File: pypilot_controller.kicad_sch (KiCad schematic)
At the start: 36 parts, among them J1 power+, J2 power-, J3 Motor A, J4 Motor B, Q1 Q_NMOS_GDS, Q2 Q_NMOS_GDS, Q3 Q_NMOS_GDS, Q4 Q_NMOS_GDS, Q5 Q_NMOS_GDS, U2 IR2101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

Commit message: Rename NCP5106B to IR2102
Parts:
- U2, U3: symbol pypilot_components:ncp5106b -> pypilot_components:IR2101
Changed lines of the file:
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@@
 	)
 	(symbol
-		(lib_id "pypilot_components:ncp5106b")
+		(lib_id "pypilot_components:IR2101")
 		(at 138.43 73.66 0)
 		(unit 1)
@@
 	)
 	(symbol
-		(lib_id "pypilot_components:ncp5106b")
+		(lib_id "pypilot_components:IR2101")
 		(at 138.43 104.14 0)
 		(unit 1)

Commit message: Added tooling holes for JLC's assembly service
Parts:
- added T1, T2, T3: Tooling, pypilot_controller_footprints:JLC_Tooling_Hole, symbol pypilot_components:Tooling
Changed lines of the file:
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@@
 		(on_board yes)
 		(dnp no)
-		(property "Reference" "#PWR22"
+		(property "Reference" "#PWR022"
 			(at 186.69 73.66 0)
 			(effects
@@
 			(project "pypilot_controller"
 				(path "/3485d22d-0932-4f13-a5db-09c3f9bc7038"
-					(reference "#PWR22")
+					(reference "#PWR022")
 					(unit 1)
 				)
@@
 		(on_board yes)
 		(dnp no)
-		(property "Reference" "#PWR125"
+		(property "Reference" "#PWR0125"
 			(at 59.69 92.71 0)
 			(effects
@@
 			(project "pypilot_controller"
 				(path "/3485d22d-0932-4f13-a5db-09c3f9bc7038"
-					(reference "#PWR125")
+					(reference "#PWR0125")
 					(unit 1)
 				)
@@
 	)
 	(symbol
+		(lib_id "pypilot_components:Tooling")
+		(at 36.83 193.04 0)
+		(unit 1)
+		(exclude_from_sim no)
+		(in_bom no)
+		(on_board yes)
+		(dnp no)
+		(fields_autoplaced yes)
+		(property "Reference" "T3"
+			(at 38.989 191.8278 0)
+			(effects
+				(font
+					(size 1.27 1.27)
+				)
+				(justify left)
+			)
+		)
+		(property "Value" "Tooling"
+			(at 38.989 194.2521 0)
+			(effects
+				(font
+					(size 1.27 1.27)
+				)
+				(justify left)
+			)
+		)
+		(property "Footprint" "pypilot_controller_footprints:JLC_Tooling_Hole"
+			(at 39.37 195.58 0)
+			(effects
+				(font
+					(size 1.27 1.27)
+				)
+				(hide yes)
+			)
+		)
+		(property "Datasheet" "~"
+			(at 36.83 193.04 0)
+			(effects
+				(font
+					(size 1.27 1.27)
+				)
+				(hide yes)
+			)
+		)
+		(property "Description" "JLC tooling hole"
+			(at 36.83 193.04 0)
+			(effects
+				(font
+					(size 1.27 1.27)
+				)
+				(hide yes)
+			)
+		)
+		(instances
+			(project ""
+				(path "/3485d22d-0932-4f13-a5db-09c3f9bc7038"
+					(reference "T3")
+					(unit 1)
+				)
+			)
+		)
+	)
+	(symbol
+		(lib_id "pypilot_components:Tooling")
+		(at 36.83 187.96 0)
+		(unit 1)
+		(exclude_from_sim no)
+		(in_bom no)
+		(on_board yes)
+		(dnp no)
+		(fields_autoplaced yes)
+		(property "Reference" "T2"
+			(at 38.989 186.7478 0)
+			(effects
+				(font
+					(size 1.27 1.27)
+				)
+				(justify left)
+			)
+		)
+		(property "Value" "Tooling"
+			(at 38.989 189.1721 0)
+			(effects
+				(font
+					(size 1.27 1.27)
+				)
+				(justify left)
+			)
+		)
+		(property "Footprint" "pypilot_controller_footprints:JLC_Tooling_Hole"
+			(at 39.37 190.5 0)
+			(effects
+				(font
+					(size 1.27 1.27)
+				)
+				(hide yes)
+			)
+		)
+		(property "Datasheet" "~"
+			(at 36.83 187.96 0)
+			(effects
+				(font
+					(size 1.27 1.27)
+				)
+				(hide yes)
+			)
+		)
+		(property "Description" "JLC tooling hole"
+			(at 36.83 187.96 0)
+			(effects
+				(font
+					(size 1.27 1.27)
+				)
+				(hide yes)
+			)
+		)
+		(instances
+			(project "pypilot_controller"
+				(path "/3485d22d-0932-4f13-a5db-09c3f9bc7038"
+					(reference "T2")
+					(unit 1)
+				)
+			)
+		)
+	)
+	(symbol
 		(lib_id "Mechanical:MountingHole")
 		(at 17.78 193.04 0)
@@
 					(unit 1)
 				)
+			)
+		)
+	)
+	(symbol
+		(lib_id "pypilot_components:Tooling")
+		(at 36.83 182.88 0)
+		(unit 1)
+		(exclude_from_sim no)
+		(in_bom no)
+		(on_board yes)
+		(dnp no)
+		(fields_autoplaced yes)
+		(property "Reference" "T1"
+			(at 38.989 181.6678 0)
+			(effects
+				(font
+					(size 1.27 1.27)
+				)
+				(justify left)
+			)
+		)
+		(property "Value" "Tooling"
+			(at 38.989 184.0921 0)
+			(effects
+				(font
+					(size 1.27 1.27)
+				)
+				(justify left)
+			)
+		)
+		(property "Footprint" "pypilot_controller_footprints:JLC_Tooling_Hole"
+			(at 39.37 185.42 0)
+			(effects
+				(font
+					(size 1.27 1.27)
+				)
+				(hide yes)
+			)
+		)
+		(property "Datasheet" "~"
+			(at 36.83 182.88 0)
+			(effects
+				(font
+					(size 1.27 1.27)
+				)
+				(hide yes)
+			)
+		)
+		(property "Description" "JLC tooling hole"
+			(at 36.83 182.88 0)
+			(effects
+				(font
+					(size 1.27 1.27)
+				)
+				(hide yes)
+			)
+		)
+		(instances
+			(project "pypilot_controller"
+				(path "/3485d22d-0932-4f13-a5db-09c3f9bc7038"
+					(reference "T1")
+					(unit 1)
+				)

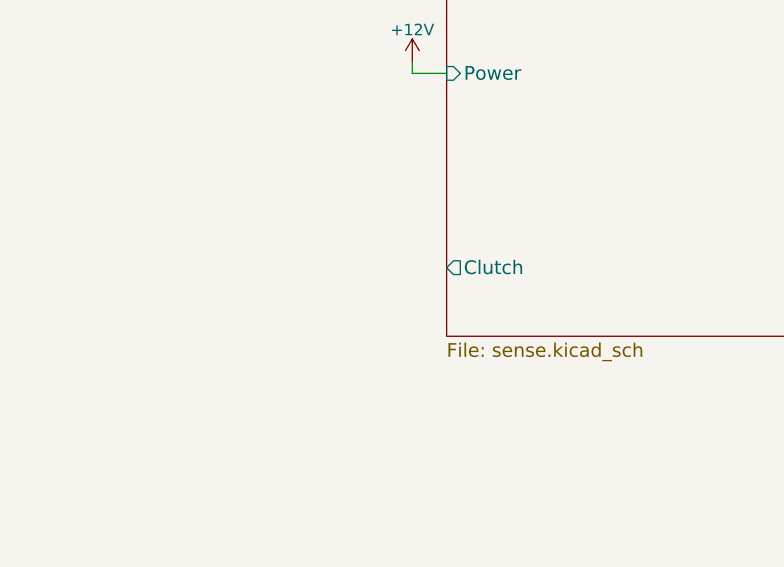
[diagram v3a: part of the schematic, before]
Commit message: Break out clutch pin to header
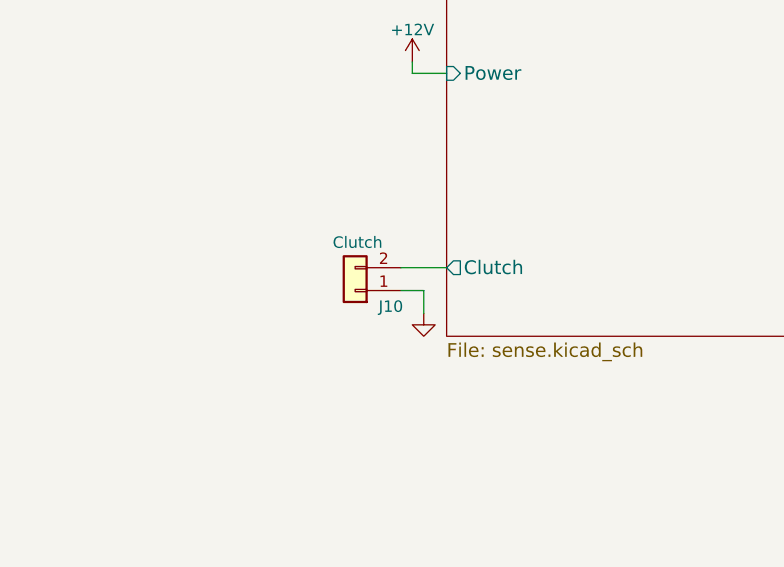
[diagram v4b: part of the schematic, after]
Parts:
- added J10: Clutch, Connector_PinHeader_2.54mm:PinHeader_1x02_P2.54mm_Vertical, symbol Connector_Generic:Conn_01x02
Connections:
- net GND: now also J10.1 (Pin_1)
- net sense/Clutch: now also J10.2 (Pin_2)
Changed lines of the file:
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@@
 	(wire
 		(pts
+			(xy 58.42 114.3) (xy 60.96 114.3)
+		)
+		(stroke
+			(width 0)
+			(type default)
+		)
+	)
+	(wire
+		(pts
 			(xy 124.46 102.87) (xy 124.46 106.68)
 		)
@@
 	(wire
 		(pts
+			(xy 60.96 114.3) (xy 60.96 116.84)
+		)
+		(stroke
+			(width 0)
+			(type default)
+		)
+	)
+	(wire
+		(pts
 			(xy 165.1 80.01) (xy 165.1 74.93)
 		)
@@
 	(wire
 		(pts
+			(xy 58.42 111.76) (xy 63.5 111.76)
+		)
+		(stroke
+			(width 0)
+			(type default)
+		)
+	)
+	(wire
+		(pts
 			(xy 128.27 85.09) (xy 123.19 85.09)
 		)
@@
 	)
 	(symbol
+		(lib_id "Connector_Generic:Conn_01x02")
+		(at 53.34 114.3 180)
+		(unit 1)
+		(exclude_from_sim no)
+		(in_bom yes)
+		(on_board yes)
+		(dnp no)
+		(property "Reference" "J10"
+			(at 58.674 116.078 0)
+			(effects
+				(font
+					(size 1.27 1.27)
+				)
+				(justify left)
+			)
+		)
+		(property "Value" "Clutch"
+			(at 56.388 108.966 0)
+			(effects
+				(font
+					(size 1.27 1.27)
+				)
+				(justify left)
+			)
+		)
+		(property "Footprint" "Connector_PinHeader_2.54mm:PinHeader_1x02_P2.54mm_Vertical"
+			(at 53.34 114.3 0)
+			(effects
+				(font
+					(size 1.27 1.27)
+				)
+				(hide yes)
+			)
+		)
+		(property "Datasheet" "~"
+			(at 53.34 114.3 0)
+			(effects
+				(font
+					(size 1.27 1.27)
+				)
+				(hide yes)
+			)
+		)
+		(property "Description" "Generic connector, single row, 01x02, script generated (kicad-library-utils/schlib/autogen/connector/)"
+			(at 53.34 114.3 0)
+			(effects
+				(font
+					(size 1.27 1.27)
+				)
+				(hide yes)
+			)
+		)
+		(pin "1"
+		)
+		(pin "2"
+		)
+		(instances
+			(project "pypilot_controller"
+				(path "/3485d22d-0932-4f13-a5db-09c3f9bc7038"
+					(reference "J10")
+					(unit 1)
+				)
+			)
+		)
+	)
+	(symbol
 		(lib_id "Mechanical:MountingHole")
 		(at 17.78 182.88 0)
@@
 					(unit 1)
 				)
+			)
+		)
+	)
+	(symbol
+		(lib_id "power:GND")
+		(at 60.96 116.84 0)
+		(unit 1)
+		(exclude_from_sim no)
+		(in_bom yes)
+		(on_board yes)
+		(dnp no)
+		(property "Reference" "#PWR03"
+			(at 60.96 123.19 0)
+			(effects
+				(font
+					(size 1.27 1.27)
+				)
+				(hide yes)
+			)
+		)
+		(property "Value" "GND"
+			(at 57.15 118.11 0)
+			(effects
+				(font
+					(size 1.27 1.27)
+				)
+				(hide yes)
+			)
+		)
+		(property "Footprint" ""
+			(at 60.96 116.84 0)
+			(effects
+				(font
+					(size 1.27 1.27)
+				)
+				(hide yes)
+			)
+		)
+		(property "Datasheet" ""
+			(at 60.96 116.84 0)
+			(effects
+				(font
+					(size 1.27 1.27)
+				)
+				(hide yes)
+			)
+		)
+		(property "Description" "Power symbol creates a global label with name \"GND\" , ground"
+			(at 60.96 116.84 0)
+			(effects
+				(font
+					(size 1.27 1.27)
+				)
+				(hide yes)
+			)
+		)
+		(pin "1"
+		)
+		(instances
+			(project "pypilot_controller"
+				(path "/3485d22d-0932-4f13-a5db-09c3f9bc7038"
+					(reference "#PWR03")
+					(unit 1)
+				)

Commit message: Change TO-252 footprint to use less solder paste
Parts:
- Q1, Q2, Q3, Q4, Q5: footprint Package_TO_SOT_SMD:TO-252-2 -> pypilot_controller_footprints:TO-252-2-reduced-paste
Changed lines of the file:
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@@
 			)
 		)
-		(property "Footprint" "Package_TO_SOT_SMD:TO-252-2"
+		(property "Footprint" "pypilot_controller_footprints:TO-252-2-reduced-paste"
 			(at 210.82 82.55 0)
 			(effects
@@
 			)
 		)
-		(property "Footprint" "Package_TO_SOT_SMD:TO-252-2"
+		(property "Footprint" "pypilot_controller_footprints:TO-252-2-reduced-paste"
 			(at 210.82 72.39 0)
 			(effects
@@
 			)
 		)
-		(property "Footprint" "Package_TO_SOT_SMD:TO-252-2"
+		(property "Footprint" "pypilot_controller_footprints:TO-252-2-reduced-paste"
 			(at 176.53 72.39 0)
 			(effects
@@
 			)
 		)
-		(property "Footprint" "Package_TO_SOT_SMD:TO-252-2"
+		(property "Footprint" "pypilot_controller_footprints:TO-252-2-reduced-paste"
 			(at 176.53 82.55 0)
 			(effects
@@
 			)
 		)
-		(property "Footprint" "Package_TO_SOT_SMD:TO-252-2"
+		(property "Footprint" "pypilot_controller_footprints:TO-252-2-reduced-paste"
 			(at 54.61 59.69 0)
 			(effects

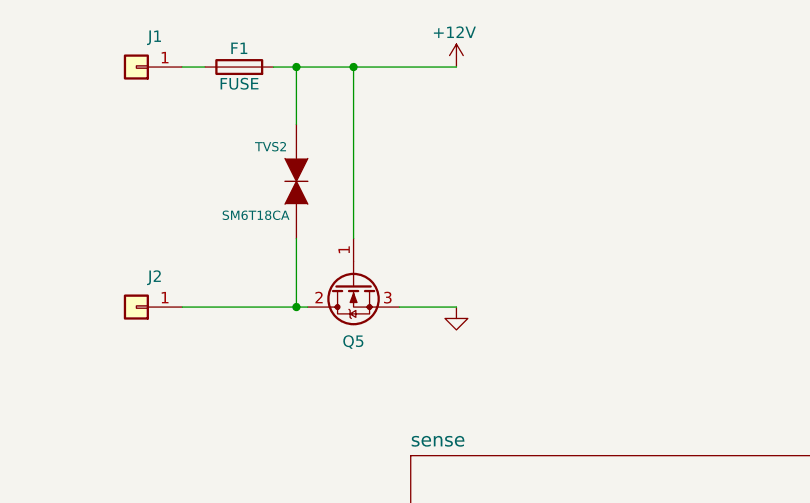
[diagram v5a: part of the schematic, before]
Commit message: Fixed almost all ERC errors and warnings (now 0 errors, 3 warnings)
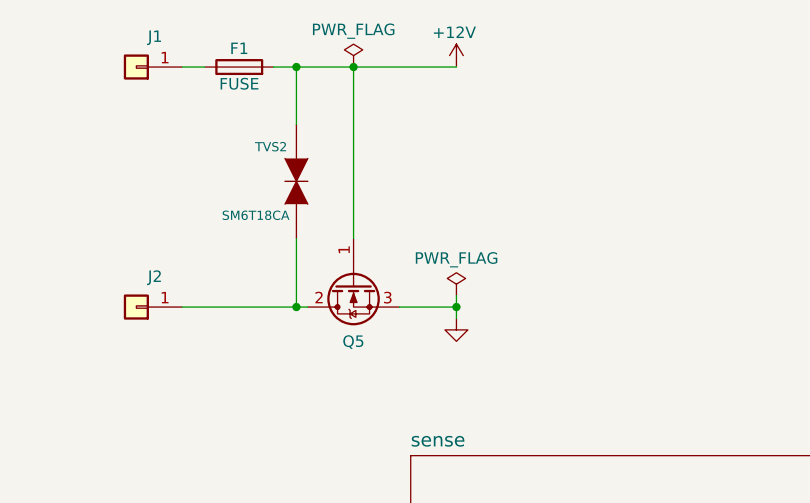
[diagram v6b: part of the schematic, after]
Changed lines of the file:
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@@
 	)
 	(junction
+		(at 68.58 57.15)
+		(diameter 0)
+		(color 0 0 0 0)
+	)
+	(junction
 		(at 50.8 57.15)
 		(diameter 0)
@@
 	(wire
 		(pts
+			(xy 68.58 58.42) (xy 68.58 57.15)
+		)
+		(stroke
+			(width 0)
+			(type default)
+		)
+	)
+	(wire
+		(pts
 			(xy 234.95 90.17) (xy 234.95 92.71)
 		)
@@
 	(wire
 		(pts
+			(xy 68.58 55.88) (xy 68.58 57.15)
+		)
+		(stroke
+			(width 0)
+			(type default)
+		)
+	)
+	(wire
+		(pts
 			(xy 128.27 72.39) (xy 128.27 77.47)
 		)
@@
 	(symbol
 		(lib_id "power:GND")
-		(at 68.58 57.15 0)
+		(at 68.58 58.42 0)
 		(unit 1)
 		(exclude_from_sim no)
@@
 		(dnp no)
 		(property "Reference" "#PWR02"
-			(at 68.58 63.5 0)
+			(at 68.58 64.77 0)
 			(effects
 				(font
@@
 		)
 		(property "Value" "GND"
-			(at 72.39 57.15 0)
+			(at 72.39 58.42 0)
 			(effects
 				(font
@@
 		)
 		(property "Footprint" ""
-			(at 68.58 57.15 0)
+			(at 68.58 58.42 0)
 			(effects
 				(font
@@
 		)
 		(property "Datasheet" ""
-			(at 68.58 57.15 0)
+			(at 68.58 58.42 0)
 			(effects
 				(font
@@
 		)
 		(property "Description" "Power symbol creates a global label with name \"GND\" , ground"
-			(at 68.58 57.15 0)
+			(at 68.58 58.42 0)
 			(effects
 				(font
@@
 	)
 	(symbol
+		(lib_id "power:PWR_FLAG")
+		(at 68.58 55.88 0)
+		(unit 1)
+		(exclude_from_sim no)
+		(in_bom yes)
+		(on_board yes)
+		(dnp no)
+		(fields_autoplaced yes)
+		(property "Reference" "#FLG02"
+			(at 68.58 53.975 0)
+			(effects
+				(font
+					(size 1.27 1.27)
+				)
+				(hide yes)
+			)
+		)
+		(property "Value" "PWR_FLAG"
+			(at 68.58 51.7469 0)
+			(effects
+				(font
+					(size 1.27 1.27)
+				)
+			)
+		)
+		(property "Footprint" ""
+			(at 68.58 55.88 0)
+			(effects
+				(font
+					(size 1.27 1.27)
+				)
+				(hide yes)
+			)
+		)
+		(property "Datasheet" "~"
+			(at 68.58 55.88 0)
+			(effects
+				(font
+					(size 1.27 1.27)
+				)
+				(hide yes)
+			)
+		)
+		(property "Description" "Special symbol for telling ERC where power comes from"
+			(at 68.58 55.88 0)
+			(effects
+				(font
+					(size 1.27 1.27)
+				)
+				(hide yes)
+			)
+		)
+		(pin "1"
+		)
+		(instances
+			(project "pypilot_controller"
+				(path "/3485d22d-0932-4f13-a5db-09c3f9bc7038"
+					(reference "#FLG02")
+					(unit 1)
+				)
+			)
+		)
+	)
+	(symbol
 		(lib_id "Mechanical:MountingHole")
 		(at 17.78 167.64 0)
@@
 					(unit 1)
 				)
+			)
+		)
+	)
+	(symbol
+		(lib_id "power:PWR_FLAG")
+		(at 57.15 30.48 0)
+		(unit 1)
+		(exclude_from_sim no)
+		(in_bom yes)
+		(on_board yes)
+		(dnp no)
+		(fields_autoplaced yes)
+		(property "Reference" "#FLG01"
+			(at 57.15 28.575 0)
+			(effects
+				(font
+					(size 1.27 1.27)
+				)
+				(hide yes)
+			)
+		)
+		(property "Value" "PWR_FLAG"
+			(at 57.15 26.3469 0)
+			(effects
+				(font
+					(size 1.27 1.27)
+				)
+			)
+		)
+		(property "Footprint" ""
+			(at 57.15 30.48 0)
+			(effects
+				(font
+					(size 1.27 1.27)
+				)
+				(hide yes)
+			)
+		)
+		(property "Datasheet" "~"
+			(at 57.15 30.48 0)
+			(effects
+				(font
+					(size 1.27 1.27)
+				)
+				(hide yes)
+			)
+		)
+		(property "Description" "Special symbol for telling ERC where power comes from"
+			(at 57.15 30.48 0)
+			(effects
+				(font
+					(size 1.27 1.27)
+				)
+				(hide yes)
+			)
+		)
+		(pin "1"
+		)
+		(instances
+			(project ""
+				(path "/3485d22d-0932-4f13-a5db-09c3f9bc7038"
+					(reference "#FLG01")
+					(unit 1)
+				)

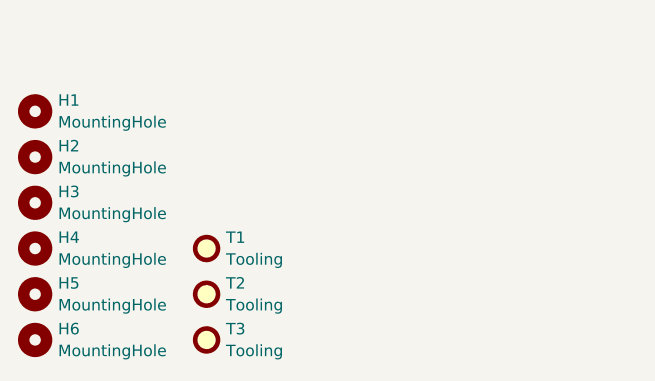
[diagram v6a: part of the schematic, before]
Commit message: Removed as many DRC errors and warnings as I could
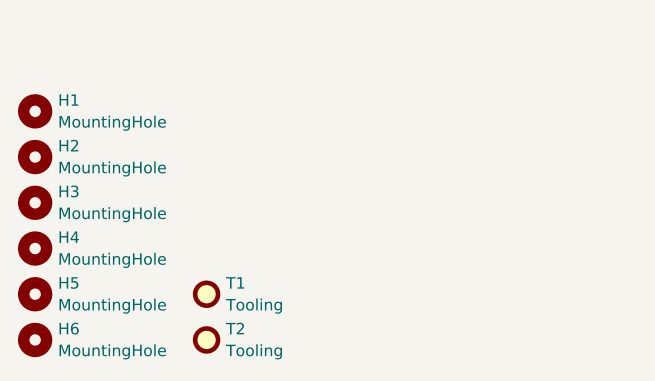
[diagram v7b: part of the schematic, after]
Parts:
- removed T2: Tooling, pypilot_controller_footprints:JLC_Tooling_Hole, symbol pypilot_components:Tooling
- renumbered T3 to T2
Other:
- moved on the sheet: T1
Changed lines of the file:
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@@
 		(dnp no)
 		(fields_autoplaced yes)
-		(property "Reference" "T3"
+		(property "Reference" "T2"
 			(at 38.989 191.8278 0)
 			(effects
@@
 		(instances
 			(project ""
-				(path "/3485d22d-0932-4f13-a5db-09c3f9bc7038"
-					(reference "T3")
-					(unit 1)
-				)
-			)
-		)
-	)
-	(symbol
-		(lib_id "pypilot_components:Tooling")
-		(at 36.83 187.96 0)
-		(unit 1)
-		(exclude_from_sim no)
-		(in_bom no)
-		(on_board yes)
-		(dnp no)
-		(fields_autoplaced yes)
-		(property "Reference" "T2"
-			(at 38.989 186.7478 0)
-			(effects
-				(font
-					(size 1.27 1.27)
-				)
-				(justify left)
-			)
-		)
-		(property "Value" "Tooling"
-			(at 38.989 189.1721 0)
-			(effects
-				(font
-					(size 1.27 1.27)
-				)
-				(justify left)
-			)
-		)
-		(property "Footprint" "pypilot_controller_footprints:JLC_Tooling_Hole"
-			(at 39.37 190.5 0)
-			(effects
-				(font
-					(size 1.27 1.27)
-				)
-				(hide yes)
-			)
-		)
-		(property "Datasheet" "~"
-			(at 36.83 187.96 0)
-			(effects
-				(font
-					(size 1.27 1.27)
-				)
-				(hide yes)
-			)
-		)
-		(property "Description" "JLC tooling hole"
-			(at 36.83 187.96 0)
-			(effects
-				(font
-					(size 1.27 1.27)
-				)
-				(hide yes)
-			)
-		)
-		(instances
-			(project "pypilot_controller"
 				(path "/3485d22d-0932-4f13-a5db-09c3f9bc7038"
 					(reference "T2")
@@
 	(symbol
 		(lib_id "pypilot_components:Tooling")
-		(at 36.83 182.88 0)
+		(at 36.83 187.96 0)
 		(unit 1)
 		(exclude_from_sim no)
@@
 		(fields_autoplaced yes)
 		(property "Reference" "T1"
-			(at 38.989 181.6678 0)
+			(at 38.989 186.7478 0)
 			(effects
 				(font
@@
 		)
 		(property "Value" "Tooling"
-			(at 38.989 184.0921 0)
+			(at 38.989 189.1721 0)
 			(effects
 				(font
@@
 		)
 		(property "Footprint" "pypilot_controller_footprints:JLC_Tooling_Hole"
-			(at 39.37 185.42 0)
-			(effects
-				(font
-					(size 1.27 1.27)
-				)
-				(hide yes)
-			)
-		)
-		(property "Datasheet" "~"
-			(at 36.83 182.88 0)
+			(at 39.37 190.5 0)
+			(effects
+				(font
+					(size 1.27 1.27)
+				)
+				(hide yes)
+			)
+		)
+		(property "Datasheet" "~"
+			(at 36.83 187.96 0)
 			(effects
 				(font
@@
 		)
 		(property "Description" "JLC tooling hole"
-			(at 36.83 182.88 0)
-			(effects
-				(font
+			(at 36.83 187.96 0)
+			(effects
+				(font

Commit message: Cleaned LCSC part numbers out of datasheet field (and renamed 0.1u to 100n)
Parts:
- TVS1: LCSC C83327 -> *C83327, C468907
- TVS2: LCSC C83327 -> *C83327, C283478
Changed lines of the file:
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@@
 			)
 		)
-		(property "Datasheet" ""
+		(property "Datasheet" "~"
 			(at 138.43 73.66 0)
 			(effects
@@
 			)
 		)
-		(property "Datasheet" ""
+		(property "Datasheet" "~"
 			(at 138.43 104.14 0)
 			(effects
@@
 			)
 		)
-		(property "Datasheet" "C468907"
+		(property "Datasheet" "~"
 			(at 198.12 86.36 0)
 			(effects
@@
 			)
 		)
-		(property "LCSC" "C83327"
+		(property "LCSC" "*C83327, C468907 "
 			(at 196.85 86.36 0)
 			(effects
@@
 			)
 		)
-		(property "Datasheet" "C283478"
+		(property "Datasheet" "~"
 			(at 50.8 44.45 0)
 			(effects
@@
 			)
 		)
-		(property "LCSC" "C83327"
+		(property "LCSC" "*C83327, C283478"
 			(at 50.8 43.18 0)
 			(effects
